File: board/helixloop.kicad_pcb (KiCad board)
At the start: 2 copper layers, 144 x 144 mm, 357 parts

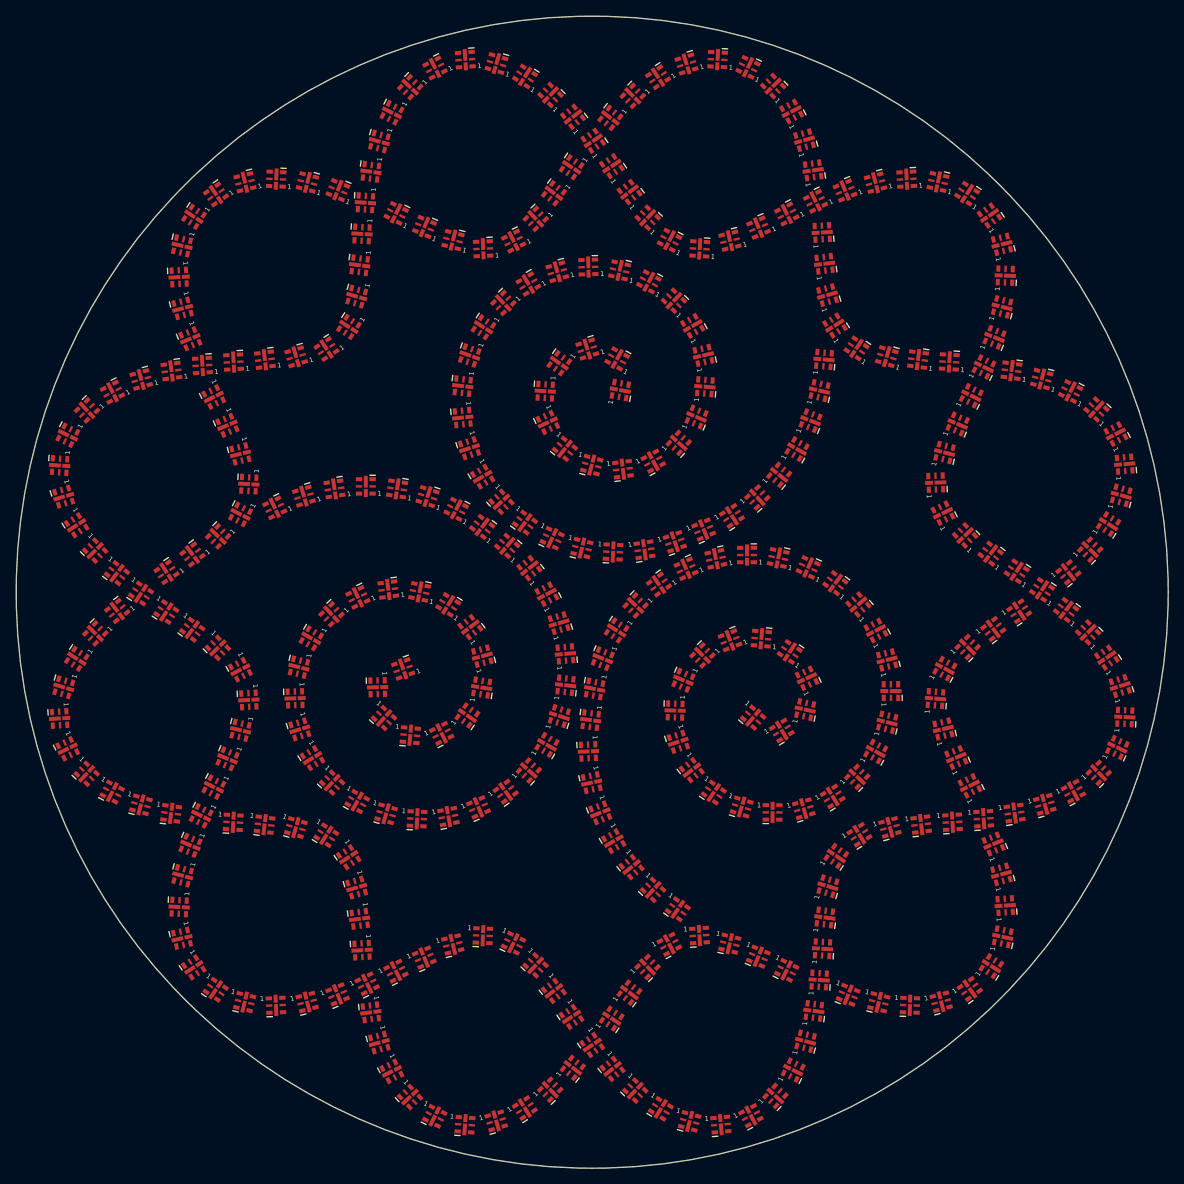
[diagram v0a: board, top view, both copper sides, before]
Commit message: adopt SK9822-EC20 led with a custom footprint; this changes the pixel spacing I thought I had, and now I want to tighten it
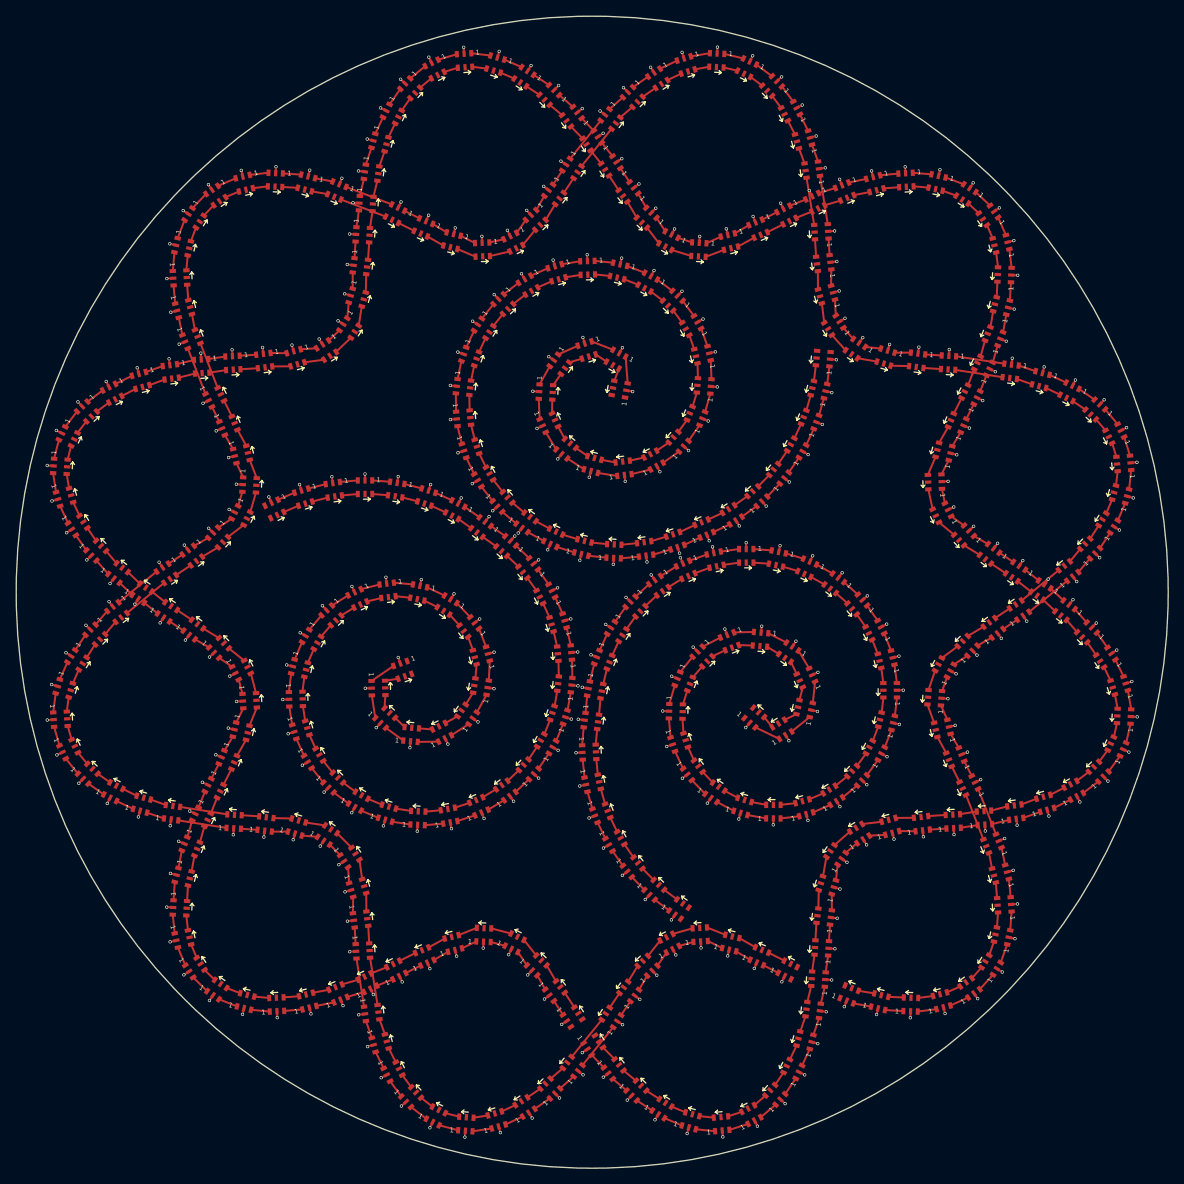
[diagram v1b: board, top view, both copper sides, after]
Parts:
- D1, D10, D100, D101, D102, D103, D104, D105, D106, D107, D108, D109, D11, D110, D111, D112, D113, D114, D115, D116, D117, D118, D119, D12, D120, D122, D123, D124, D125, D126, D127, D128, D129, D13, D130, D131, D133, D134, D135, D136, D137, D138, D139, D14, D140, D142, D143, D144, D145, D146, D147, D148, D149, D15, D150, D151, D153, D154, D155, D156, D157, D158, D159, D16, D160, D162, D163, D164, D165, D166, D167, D168, D169, D17, D170, D171, D173, D174, D175, D176, D177, D178, D179, D18, D180, D182, D183, D184, D185, D186, D187, D188, D189, D19, D190, D191, D193, D194, D195, D196, D197, D198, D199, D2, D20, D200, D202, D203, D204, D205, D206, D207, D208, D209, D21, D210, D211, D213, D214, D215, D216, D217, D218, D219, D22, D220, D222, D223, D224, D225, D226, D227, D228, D229, D23, D230, D231, D233, D234, D235, D236, D237, D238, D239, D24, D240, D241, D242, D243, D244, D245, D246, D247, D248, D249, D25, D250, D251, D252, D253, D254, D255, D256, D257, D258, D259, D26, D260, D261, D262, D263, D264, D265, D266, D267, D268, D269, D27, D270, D271, D272, D273, D274, D275, D276, D277, D278, D279, D28, D280, D281, D282, D283, D284, D285, D286, D287, D288, D289, D29, D290, D291, D292, D293, D294, D295, D296, D297, D298, D299, D3, D30, D300, D301, D302, D303, D304, D305, D306, D307, D308, D309, D31, D310, D311, D312, D313, D314, D315, D316, D317, D318, D319, D32, D320, D321, D322, D323, D324, D325, D326, D327, D328, D329, D33, D330, D331, D332, D333, D334, D335, D336, D337, D338, D339, D34, D340, D341, D342, D343, D344, D345, D346, D347, D348, D349, D35, D350, D351, D352, D353, D354, D355, D356, D357, D358, D359, D36, D360, D361, D362, D363, D364, D365, D366, D367, D368, D369, D37, D38, D39, D4, D40, D41, D42, D43, D44, D45, D46, D47, D48, D49, D5, D50, D51, D52, D53, D54, D55, D56, D57, D58, D59, D6, D60, D61, D62, D63, D64, D65, D66, D67, D68, D69, D7, D70, D71, D72, D73, D74, D75, D76, D77, D78, D79, D8, D80, D81, D82, D83, D84, D85, D86, D87, D88, D89, D9, D90, D91, D92, D93, D94, D95, D96, D97, D98, D99: value LED-APA102-2020 -> LED-SK9822-EC20; footprint LED-APA102-2020 -> LED-SK9822-EC20
- turned D1 to 123.85 degrees
- turned D10 to -104.78 degrees
- turned D100 to 63.4081 degrees
- turned D101 to 63.6343 degrees
- turned D102 to 67.5701 degrees
- turned D103 to 75.213 degrees
- turned D104 to 86.8443 degrees
- turned D105 to 102.864 degrees
- turned D106 to 123.228 degrees
- turned D107 to 145.733 degrees
- turned D108 to 166.277 degrees
- turned D109 to -177.487 degrees
- turned D11 to -97.3127 degrees
- turned D110 to -165.676 degrees
- turned D111 to -157.849 degrees
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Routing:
- net (no net): track 0.00 -> 1877.3 mm, vias 0 -> 357

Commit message: tighten pixel spacing by shrinking the entire design slightly; improve pixel layout using a square footprint; but: there's a way to make this easier
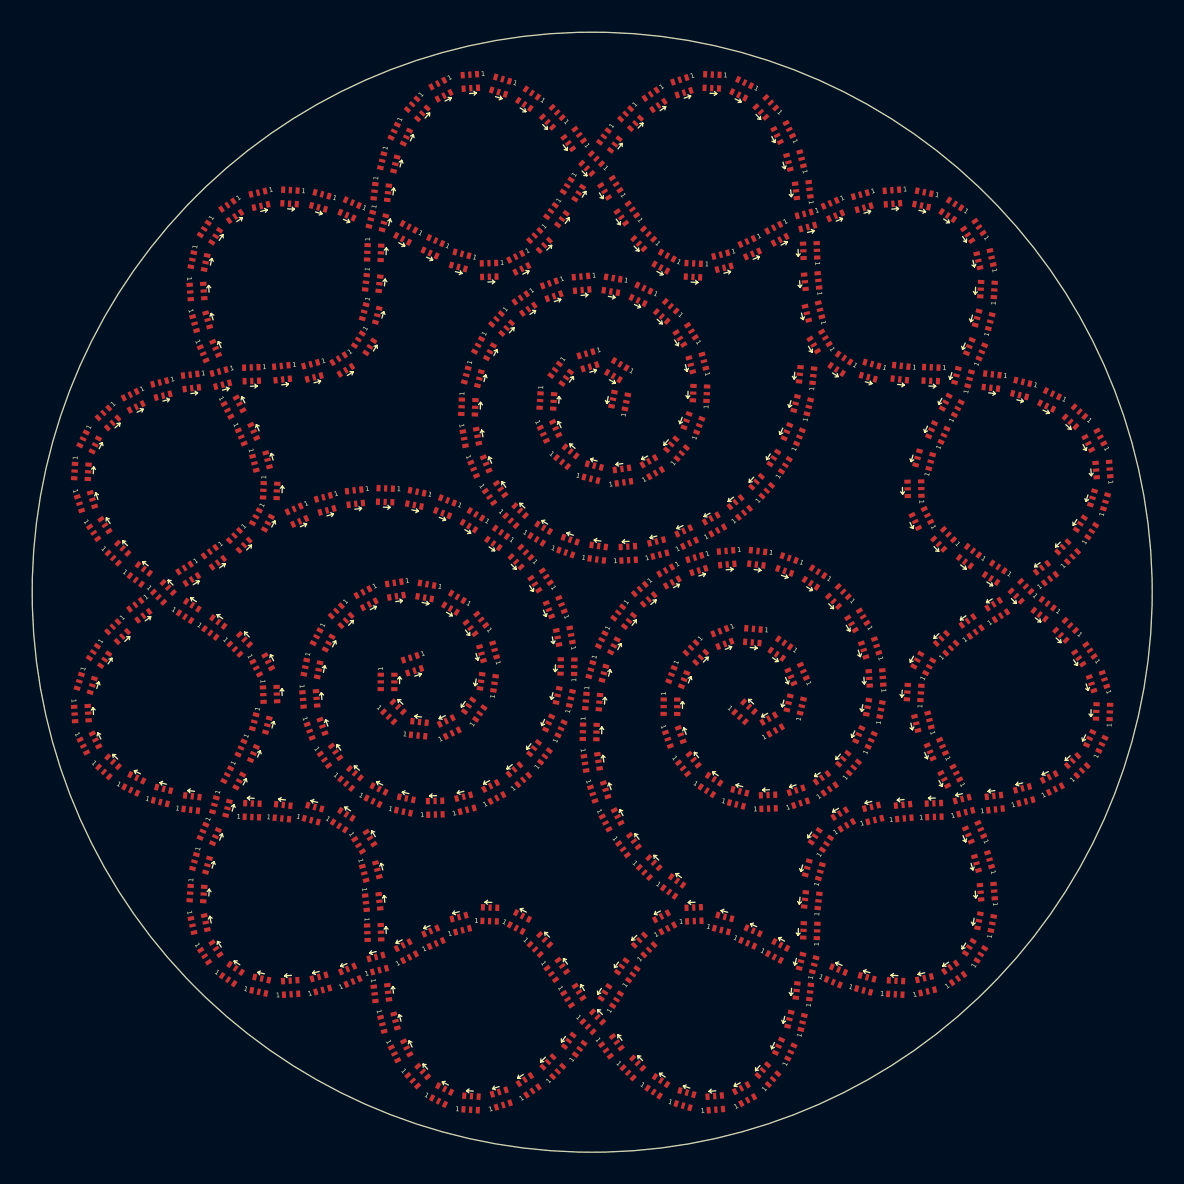
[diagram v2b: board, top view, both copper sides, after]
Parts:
- removed D367, D368, D369: LED-SK9822-EC20, LED-SK9822-EC20
- moved D326 46.1 mm to (103.1, 72.2), turned to -30.1657 degrees
- moved D283 45.2 mm to (77.5, 109.0), turned to 18.4415 degrees
- moved D325 41.2 mm to (103.4, 76.0), turned to -101.559 degrees
- moved D351 10.3 mm to (86.0, 84.3), turned to 112.926 degrees
- moved D352 10.3 mm to (87.9, 87.6), turned to 125.172 degrees
- moved D350 10.2 mm to (84.8, 80.7), turned to 100.45 degrees
- moved D353 10.2 mm to (90.4, 90.4), turned to 137.189 degrees
- moved D349 10.2 mm to (84.5, 76.9), turned to 87.7268 degrees
- moved D354 10.1 mm to (93.5, 92.7), turned to 148.994 degrees
- moved D348 10.00 mm to (85.1, 73.1), turned to 74.7371 degrees
- moved D355 9.99 mm to (97.0, 94.2), turned to 160.607 degrees
- moved D356 9.85 mm to (100.7, 95.1), turned to 172.027 degrees
- moved D347 9.79 mm to (86.5, 69.5), turned to 61.4628 degrees
- moved D357 9.69 mm to (104.5, 95.1), turned to -176.737 degrees
- moved D358 9.53 mm to (108.3, 94.5), turned to -165.675 degrees
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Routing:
- net (no net): track 1877.3 -> 0.00 mm, vias 357 -> 0
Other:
- board size 144 x 144 mm -> 140 x 140 mm

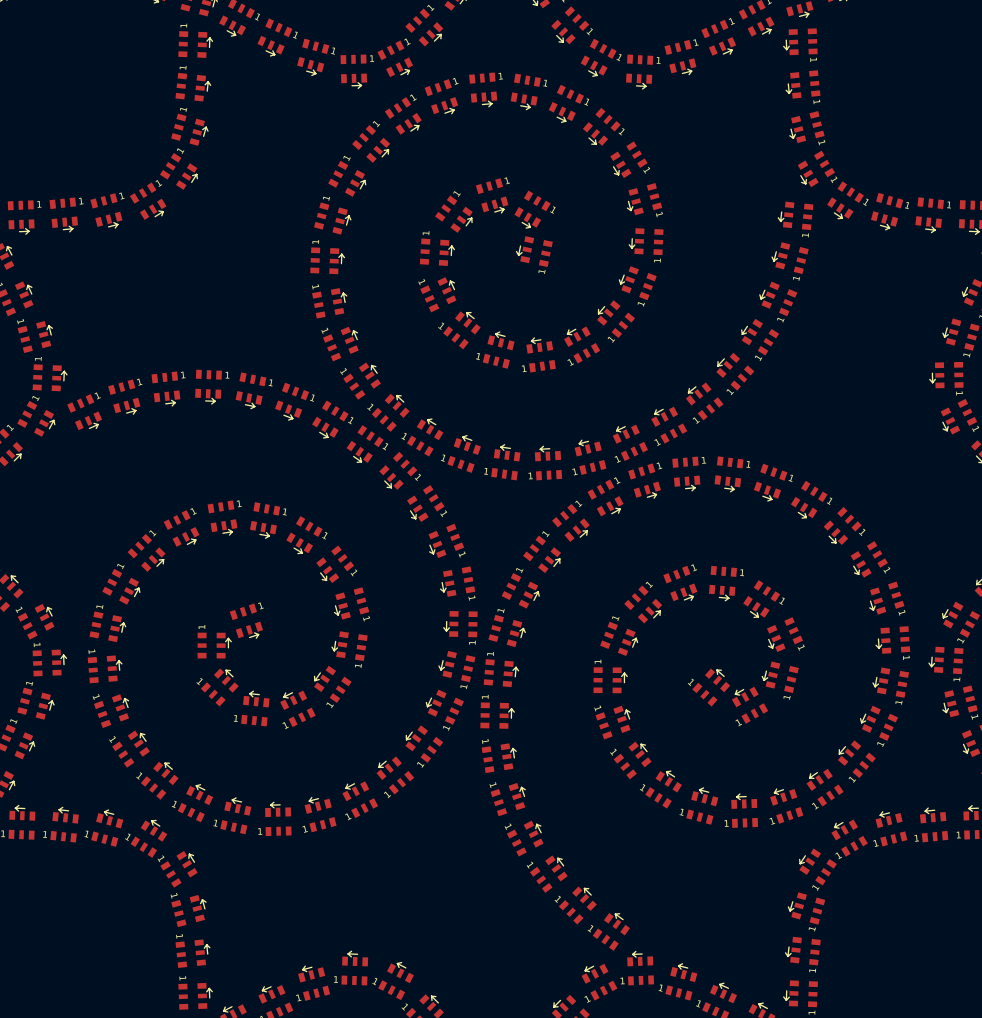
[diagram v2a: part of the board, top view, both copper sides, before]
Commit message: tweaks to spiral layout to settle on 369 pixels and align with helix
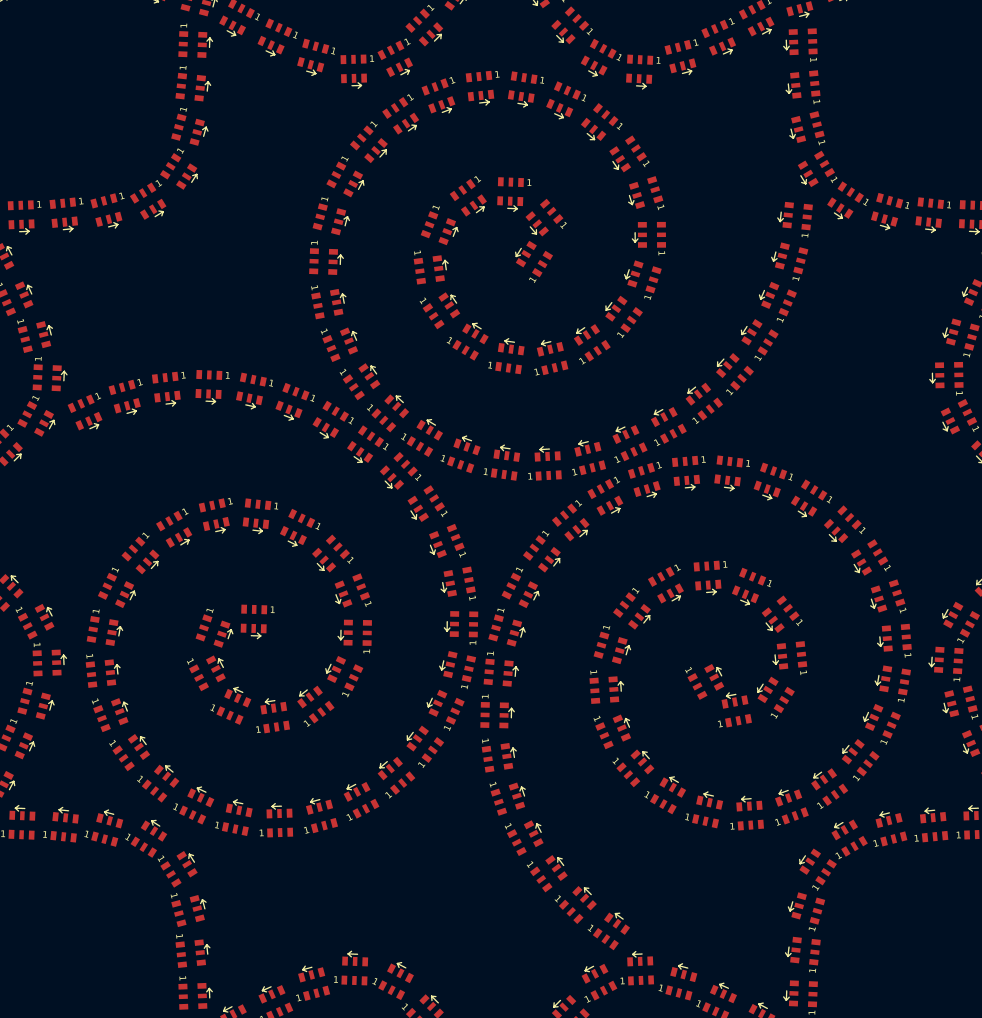
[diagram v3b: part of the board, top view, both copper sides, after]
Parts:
- added D367: LED-SK9822-EC20, LED-SK9822-EC20, F.Cu at (125.1, 80.3)
- added D368: LED-SK9822-EC20, LED-SK9822-EC20, F.Cu at (126.2, 76.6)
- added D369: LED-SK9822-EC20, LED-SK9822-EC20, F.Cu at (126.8, 72.9)
- moved D326 43.9 mm to (63.1, 90.4), turned to 24.0827 degrees
- moved D283 42.8 mm to (110.1, 136.7), turned to 144.083 degrees
- moved D325 39.0 mm to (66.7, 89.0), turned to 15.5304 degrees
- moved D361 11.4 mm to (108.2, 94.5), turned to -165.776 degrees
- moved D360 11.4 mm to (104.5, 95.2), turned to -176.832 degrees
- moved D366 11.4 mm to (123.4, 83.7), turned to -122.311 degrees
- moved D365 11.4 mm to (121.1, 86.8), turned to -131.657 degrees
- moved D362 11.4 mm to (111.8, 93.1), turned to -154.88 degrees
- moved D364 11.4 mm to (118.4, 89.4), turned to -141.315 degrees
- moved D363 11.4 mm to (115.2, 91.6), turned to -151.323 degrees
- moved D359 11.3 mm to (100.7, 95.1), turned to 171.941 degrees
- moved D358 11.3 mm to (96.9, 94.3), turned to 160.544 degrees
- moved D357 11.3 mm to (93.5, 92.7), turned to 148.959 degrees
- moved D356 11.3 mm to (90.4, 90.5), turned to 137.184 degrees
- moved D355 11.3 mm to (87.8, 87.7), turned to 125.211 degrees
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
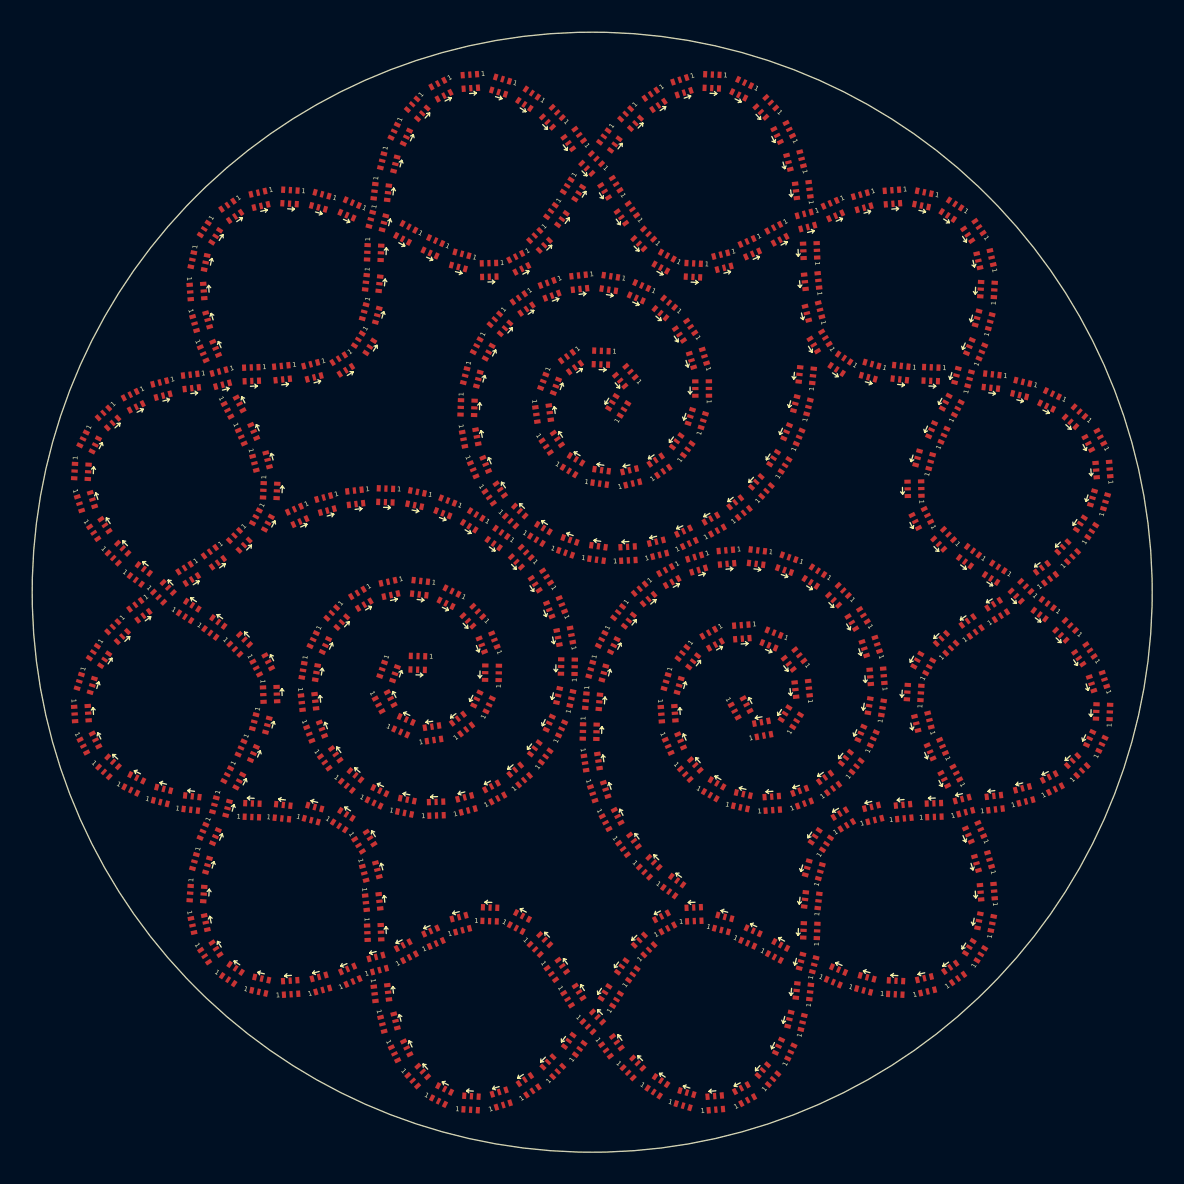
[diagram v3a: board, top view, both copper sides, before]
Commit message: improve edge cuts shape
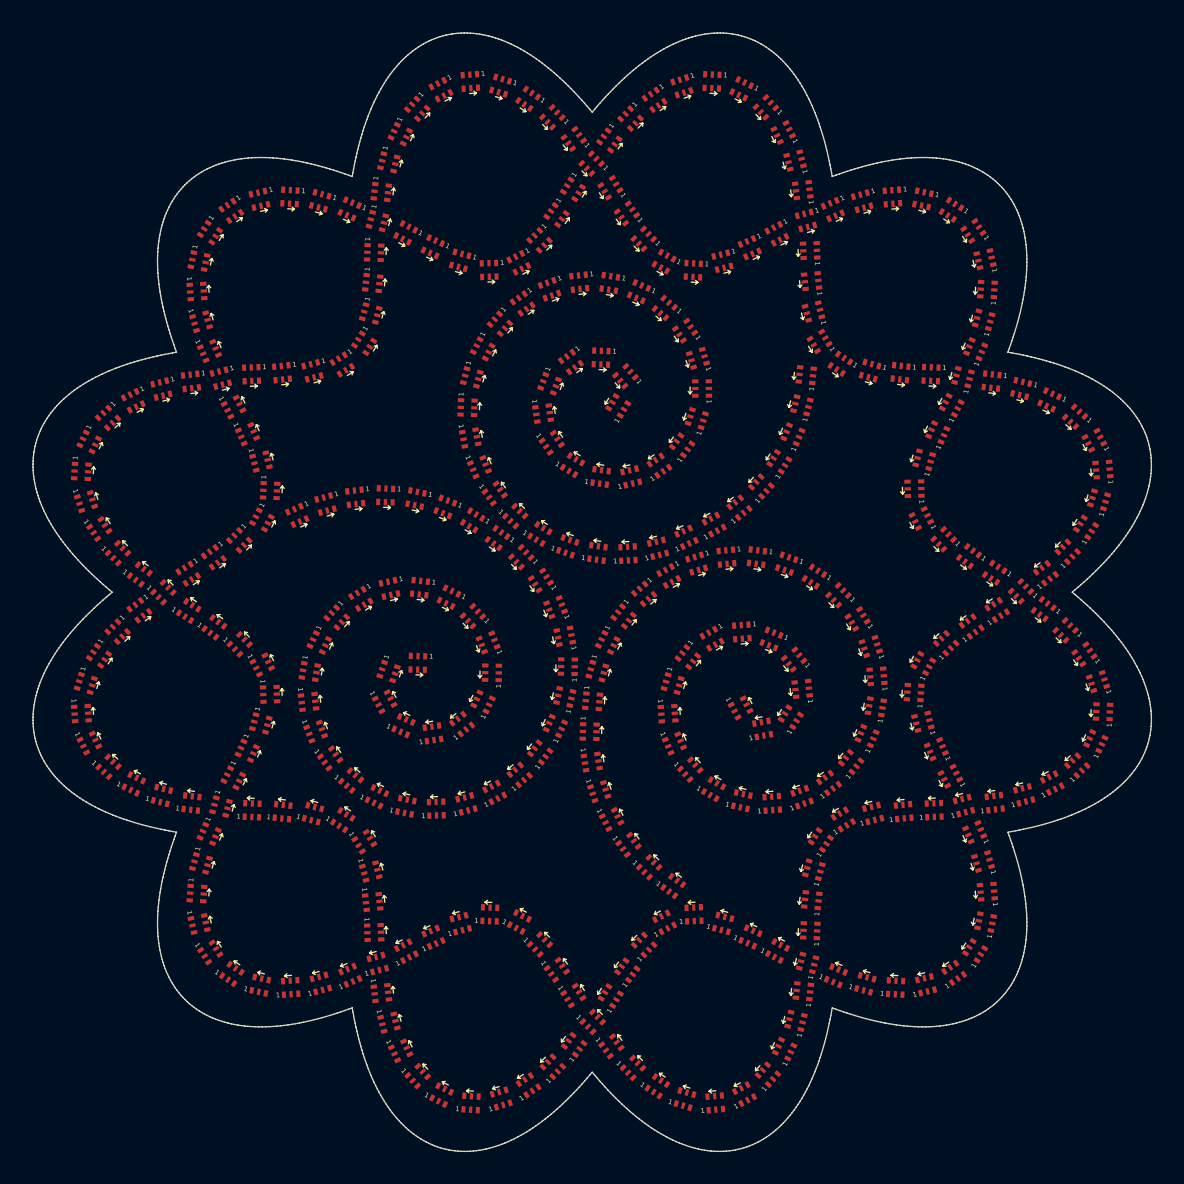
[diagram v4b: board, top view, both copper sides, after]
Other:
- board size 140 x 140 mm -> 139.8 x 139.8 mm
